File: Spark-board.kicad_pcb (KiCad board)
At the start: 2 copper layers, 45 x 40 mm, 12 parts, among them Q1 Q_NPN_EBC, Q2 Q_NPN_EBC, U1 ATMEGA328P-PU, U2 TSOP382xx

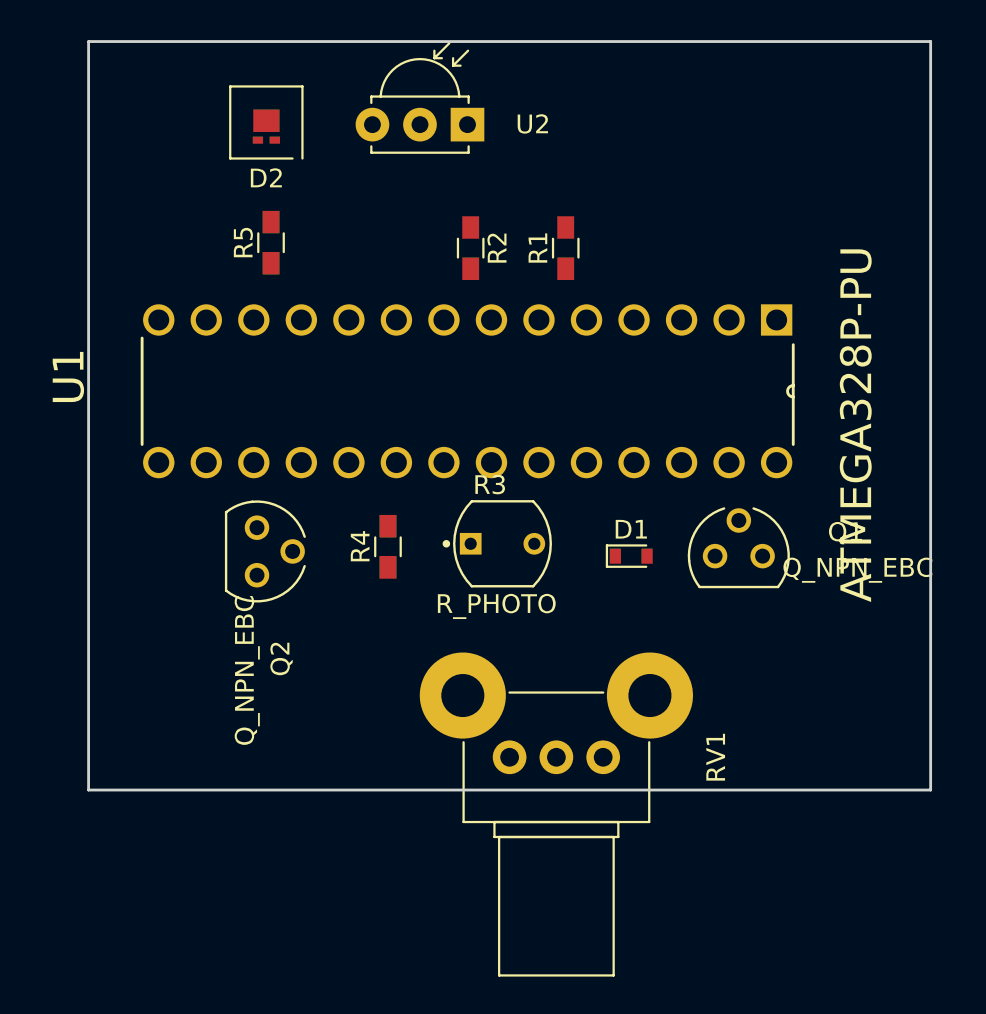
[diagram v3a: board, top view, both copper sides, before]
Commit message: Added copper track segments to PCB and translated components to the left
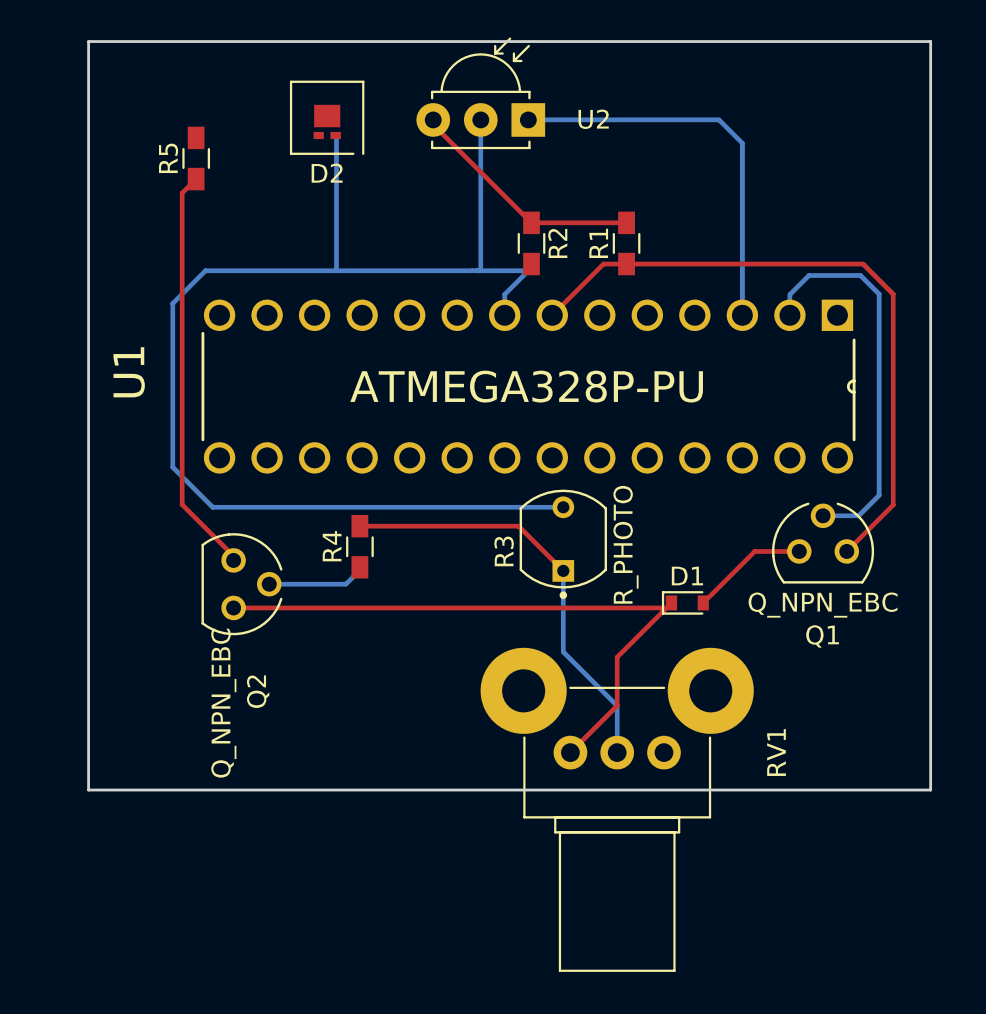
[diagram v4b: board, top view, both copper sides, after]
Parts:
- moved R5 6.02 mm to (170.8, 61.2)
- moved Q1 4.51 mm to (204.2, 82.2)
- moved D1 3.91 mm to (197.0, 85.0)
- moved D2 3.26 mm to (177.8, 59.5)
- moved R1 3.26 mm to (193.8, 65.8)
- moved R2 3.26 mm to (188.7, 65.8)
- moved R3 3.26 mm to (190.4, 81.6), turned to 90 degrees
- moved RV1 3.26 mm to (190.8, 93.0)
- moved U1 3.26 mm to (172.0, 77.2)
- moved U2 3.26 mm to (188.5, 59.2)
- moved Q2 2.15 mm to (172.8, 84.0)
- moved R4 1.50 mm to (179.5, 82.0)
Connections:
- R3 pad 2: Net-(R3-Pad2) -> GND
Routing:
- net GND: track 0.00 -> 68.7 mm
- net /5V: track 0.00 -> 34.8 mm
- net Net-(D1-Pad1): track 0.00 -> 33.0 mm
- net Net-(R3-Pad1): track 0.00 -> 22.8 mm
- net Net-(Q2-Pad1): track 0.00 -> 21.8 mm
- net /IR_RX_OUT_1: track 0.00 -> 21.1 mm
- net /Q1_SWITCH_BASE: track 0.00 -> 21.1 mm
- net Net-(R1-Pad2): track 0.00 -> 12.8 mm
- net Net-(D1-Pad2): track 0.00 -> 6.27 mm
- net Net-(Q2-Pad2): track 0.00 -> 5.16 mm
